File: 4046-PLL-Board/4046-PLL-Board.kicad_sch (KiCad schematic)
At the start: 45 parts, among them J1 Conn_01x02_Pin, J2 Conn_02x03_Odd_Even, J3 Conn_01x02_Pin, J4 Conn_01x02_Pin, J5 Conn_01x02_Pin, J6 Conn_01x03_Pin, U1 CD4046, U2 74LVC2G04, U3 L78M05

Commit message: add IXD614 GDT Driver design REV 1.0.0
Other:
- moved on the sheet: C5, LED1, LED2, R5, R6
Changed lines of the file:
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@@
 	)
 	(junction
-		(at 67.31 167.64)
+		(at 48.26 168.91)
 		(diameter 0)
 		(color 0 0 0 0)
@@
 	(wire
 		(pts
-			(xy 60.96 167.64) (xy 67.31 167.64)
+			(xy 41.91 168.91) (xy 48.26 168.91)
 		)
 		(stroke
@@
 	(wire
 		(pts
-			(xy 87.63 167.64) (xy 81.28 167.64)
+			(xy 68.58 168.91) (xy 62.23 168.91)
 		)
 		(stroke
@@
 	(wire
 		(pts
-			(xy 39.37 167.64) (xy 53.34 167.64)
+			(xy 20.32 168.91) (xy 34.29 168.91)
 		)
 		(stroke
@@
 	(wire
 		(pts
-			(xy 60.96 154.94) (xy 73.66 154.94)
+			(xy 41.91 156.21) (xy 54.61 156.21)
 		)
 		(stroke
@@
 	(wire
 		(pts
-			(xy 87.63 154.94) (xy 81.28 154.94)
+			(xy 68.58 156.21) (xy 62.23 156.21)
 		)
 		(stroke
@@
 	(wire
 		(pts
-			(xy 67.31 167.64) (xy 73.66 167.64)
+			(xy 48.26 168.91) (xy 54.61 168.91)
 		)
 		(stroke
@@
 	)
 	(label "LOCK_STATUS"
-		(at 39.37 167.64 0)
+		(at 20.32 168.91 0)
 		(effects
 			(font
@@
 	(symbol
 		(lib_id "Device:LED")
-		(at 77.47 167.64 180)
+		(at 58.42 168.91 180)
 		(unit 1)
 		(exclude_from_sim no)
@@
 		(fields_autoplaced yes)
 		(property "Reference" "LED2"
-			(at 79.0575 160.02 0)
+			(at 60.0075 161.29 0)
 			(effects
 				(font
@@
 		)
 		(property "Value" "Lock Green"
-			(at 79.0575 162.56 0)
+			(at 60.0075 163.83 0)
 			(effects
 				(font
@@
 		)
 		(property "Footprint" "LED_SMD:LED_0603_1608Metric_Pad1.05x0.95mm_HandSolder"
-			(at 77.47 167.64 0)
+			(at 58.42 168.91 0)
 			(effects
 				(font
@@
 		)
 		(property "Datasheet" "~"
-			(at 77.47 167.64 0)
+			(at 58.42 168.91 0)
 			(effects
 				(font
@@
 		)
 		(property "Description" "Light emitting diode"
-			(at 77.47 167.64 0)
+			(at 58.42 168.91 0)
 			(effects
 				(font
@@
 		)
 		(property "Sim.Pins" "1=K 2=A"
-			(at 77.47 167.64 0)
+			(at 58.42 168.91 0)
 			(effects
 				(font
@@
 	(symbol
 		(lib_id "power:GND")
-		(at 67.31 175.26 0)
+		(at 48.26 176.53 0)
 		(unit 1)
 		(exclude_from_sim no)
@@
 		(fields_autoplaced yes)
 		(property "Reference" "#PWR020"
-			(at 67.31 181.61 0)
+			(at 48.26 182.88 0)
 			(effects
 				(font
@@
 		)
 		(property "Value" "GND"
-			(at 67.31 180.34 0)
+			(at 48.26 181.61 0)
 			(effects
 				(font
@@
 		)
 		(property "Footprint" ""
-			(at 67.31 175.26 0)
+			(at 48.26 176.53 0)
 			(effects
 				(font
@@
 		)
 		(property "Datasheet" ""
-			(at 67.31 175.26 0)
+			(at 48.26 176.53 0)
 			(effects
 				(font
@@
 		)
 		(property "Description" "Power symbol creates a global label with name \"GND\" , ground"
-			(at 67.31 175.26 0)
+			(at 48.26 176.53 0)
 			(effects
 				(font
@@
 	(symbol
 		(lib_id "Device:R")
-		(at 57.15 167.64 90)
+		(at 38.1 168.91 90)
 		(unit 1)
 		(exclude_from_sim no)
@@
 		(fields_autoplaced yes)
 		(property "Reference" "R6"
-			(at 57.15 161.29 90)
+			(at 38.1 162.56 90)
 			(effects
 				(font
@@
 		)
 		(property "Value" "1k"
-			(at 57.15 163.83 90)
+			(at 38.1 165.1 90)
 			(effects
 				(font
@@
 		)
 		(property "Footprint" "Resistor_SMD:R_0603_1608Metric_Pad0.98x0.95mm_HandSolder"
-			(at 57.15 169.418 90)
+			(at 38.1 170.688 90)
 			(effects
 				(font
@@
 		)
 		(property "Datasheet" "~"
-			(at 57.15 167.64 0)
+			(at 38.1 168.91 0)
 			(effects
 				(font
@@
 		)
 		(property "Description" "Resistor"
-			(at 57.15 167.64 0)
+			(at 38.1 168.91 0)
 			(effects
 				(font
@@
 	(symbol
 		(lib_id "Device:R")
-		(at 57.15 154.94 90)
+		(at 38.1 156.21 90)
 		(unit 1)
 		(exclude_from_sim no)
@@
 		(fields_autoplaced yes)
 		(property "Reference" "R5"
-			(at 57.15 148.59 90)
+			(at 38.1 149.86 90)
 			(effects
 				(font
@@
 		)
 		(property "Value" "1k"
-			(at 57.15 151.13 90)
+			(at 38.1 152.4 90)
 			(effects
 				(font
@@
 		)
 		(property "Footprint" "Resistor_SMD:R_0603_1608Metric_Pad0.98x0.95mm_HandSolder"
-			(at 57.15 156.718 90)
+			(at 38.1 157.988 90)
 			(effects
 				(font
@@
 		)
 		(property "Datasheet" "~"
-			(at 57.15 154.94 0)
+			(at 38.1 156.21 0)
 			(effects
 				(font
@@
 		)
 		(property "Description" "Resistor"
-			(at 57.15 154.94 0)
+			(at 38.1 156.21 0)
 			(effects
 				(font
@@
 	(symbol
 		(lib_id "power:GND")
-		(at 87.63 154.94 90)
+		(at 68.58 156.21 90)
 		(unit 1)
 		(exclude_from_sim no)
@@
 		(fields_autoplaced yes)
 		(property "Reference" "#PWR014"
-			(at 93.98 154.94 0)
+			(at 74.93 156.21 0)
 			(effects
 				(font
@@
 		)
 		(property "Value" "GND"
-			(at 91.44 154.9399 90)
+			(at 72.39 156.2099 90)
 			(effects
 				(font
@@
 		)
 		(property "Footprint" ""
-			(at 87.63 154.94 0)
+			(at 68.58 156.21 0)
 			(effects
 				(font
@@
 		)
 		(property "Datasheet" ""
-			(at 87.63 154.94 0)
+			(at 68.58 156.21 0)
 			(effects
 				(font
@@
 		)
 		(property "Description" "Power symbol creates a global label with name \"GND\" , ground"
-			(at 87.63 154.94 0)
+			(at 68.58 156.21 0)
 			(effects
 				(font
@@
 	(symbol
 		(lib_id "Device:LED")
-		(at 77.47 154.94 180)
+		(at 58.42 156.21 180)
 		(unit 1)
 		(exclude_from_sim no)
@@
 		(fields_autoplaced yes)
 		(property "Reference" "LED1"
-			(at 79.0575 147.32 0)
+			(at 60.0075 148.59 0)
 			(effects
 				(font
@@
 		)
 		(property "Value" "PWR Yellow"
-			(at 79.0575 149.86 0)
+			(at 60.0075 151.13 0)
 			(effects
 				(font
@@
 		)
 		(property "Footprint" "LED_SMD:LED_0603_1608Metric_Pad1.05x0.95mm_HandSolder"
-			(at 77.47 154.94 0)
+			(at 58.42 156.21 0)
 			(effects
 				(font
@@
 		)
 		(property "Datasheet" "~"
-			(at 77.47 154.94 0)
+			(at 58.42 156.21 0)
 			(effects
 				(font
@@
 		)
 		(property "Description" "Light emitting diode"
-			(at 77.47 154.94 0)
+			(at 58.42 156.21 0)
 			(effects
 				(font
@@
 		)
 		(property "Sim.Pins" "1=K 2=A"
-			(at 77.47 154.94 0)
+			(at 58.42 156.21 0)
 			(effects
 				(font
@@
 	(symbol
 		(lib_id "power:+5V")
-		(at 53.34 154.94 90)
+		(at 34.29 156.21 90)
 		(unit 1)
 		(exclude_from_sim no)
@@
 		(fields_autoplaced yes)
 		(property "Reference" "#PWR019"
-			(at 57.15 154.94 0)
+			(at 38.1 156.21 0)
 			(effects
 				(font
@@
 		)
 		(property "Value" "+5V"
-			(at 49.53 154.9399 90)
+			(at 30.48 156.2099 90)
 			(effects
 				(font
@@
 		)
 		(property "Footprint" ""
-			(at 53.34 154.94 0)
+			(at 34.29 156.21 0)
 			(effects
 				(font
@@
 		)
 		(property "Datasheet" ""
-			(at 53.34 154.94 0)
+			(at 34.29 156.21 0)
 			(effects
 				(font
@@
 		)
 		(property "Description" "Power symbol creates a global label with name \"+5V\""
-			(at 53.34 154.94 0)
+			(at 34.29 156.21 0)
 			(effects
 				(font
@@
 	(symbol
 		(lib_id "power:GND")
-		(at 87.63 167.64 90)
+		(at 68.58 168.91 90)
 		(unit 1)
 		(exclude_from_sim no)
@@
 		(fields_autoplaced yes)
 		(property "Reference" "#PWR015"
-			(at 93.98 167.64 0)
+			(at 74.93 168.91 0)
 			(effects
 				(font
@@
 		)
 		(property "Value" "GND"
-			(at 91.44 167.6399 90)
+			(at 72.39 168.9099 90)
 			(effects
 				(font
@@
 		)
 		(property "Footprint" ""
-			(at 87.63 167.64 0)
+			(at 68.58 168.91 0)
 			(effects
 				(font
@@
 		)
 		(property "Datasheet" ""
-			(at 87.63 167.64 0)
+			(at 68.58 168.91 0)
 			(effects
 				(font
@@
 		)
 		(property "Description" "Power symbol creates a global label with name \"GND\" , ground"
-			(at 87.63 167.64 0)
+			(at 68.58 168.91 0)
 			(effects
 				(font
@@
 	(symbol
 		(lib_id "Device:C")
-		(at 67.31 171.45 180)
+		(at 48.26 172.72 180)
 		(unit 1)
 		(exclude_from_sim no)
@@
 		(fields_autoplaced yes)
 		(property "Reference" "C5"
-			(at 71.12 170.1799 0)
+			(at 52.07 171.4499 0)
 			(effects
 				(font
@@
 		)
 		(property "Value" "DNP"
-			(at 71.12 172.7199 0)
+			(at 52.07 173.9899 0)
 			(effects
 				(font
@@
 		)
 		(property "Footprint" "Capacitor_SMD:C_0603_1608Metric_Pad1.08x0.95mm_HandSolder"
-			(at 66.3448 167.64 0)
+			(at 47.2948 168.91 0)
 			(effects
 				(font
@@
 		)
 		(property "Datasheet" "~"
-			(at 67.31 171.45 0)
+			(at 48.26 172.72 0)
 			(effects
 				(font
@@
 		)
 		(property "Description" "Unpolarized capacitor"
-			(at 67.31 171.45 0)
+			(at 48.26 172.72 0)
 			(effects
 				(font

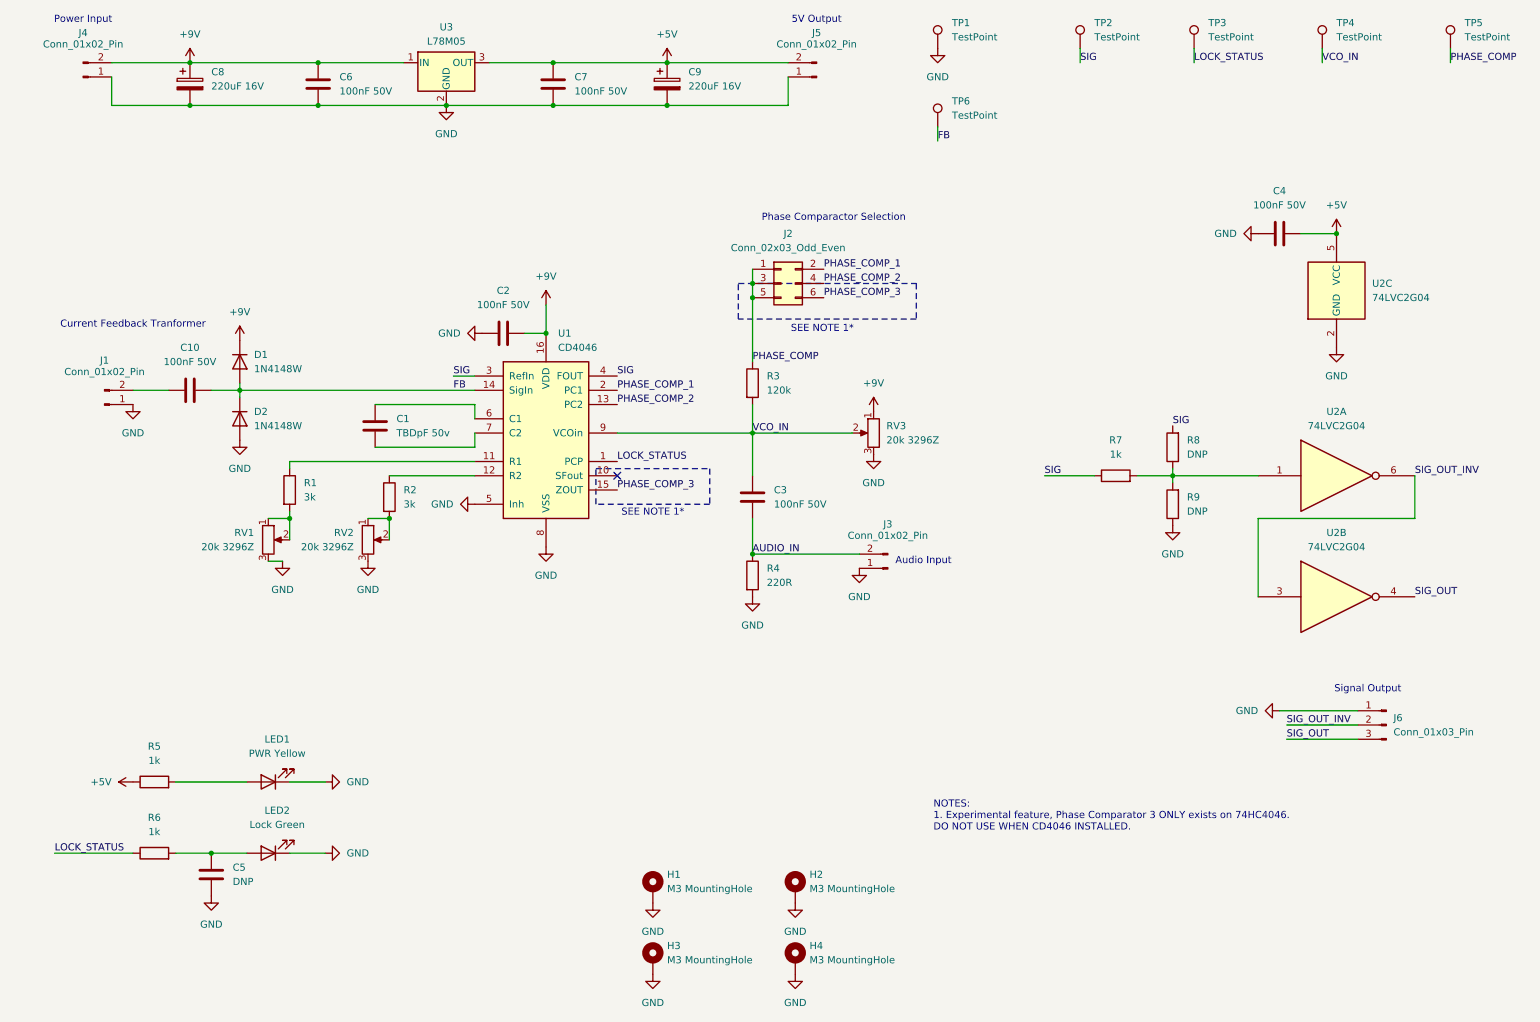
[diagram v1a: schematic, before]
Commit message: add support for CD4046 in SO-16-208mil package on PLL board
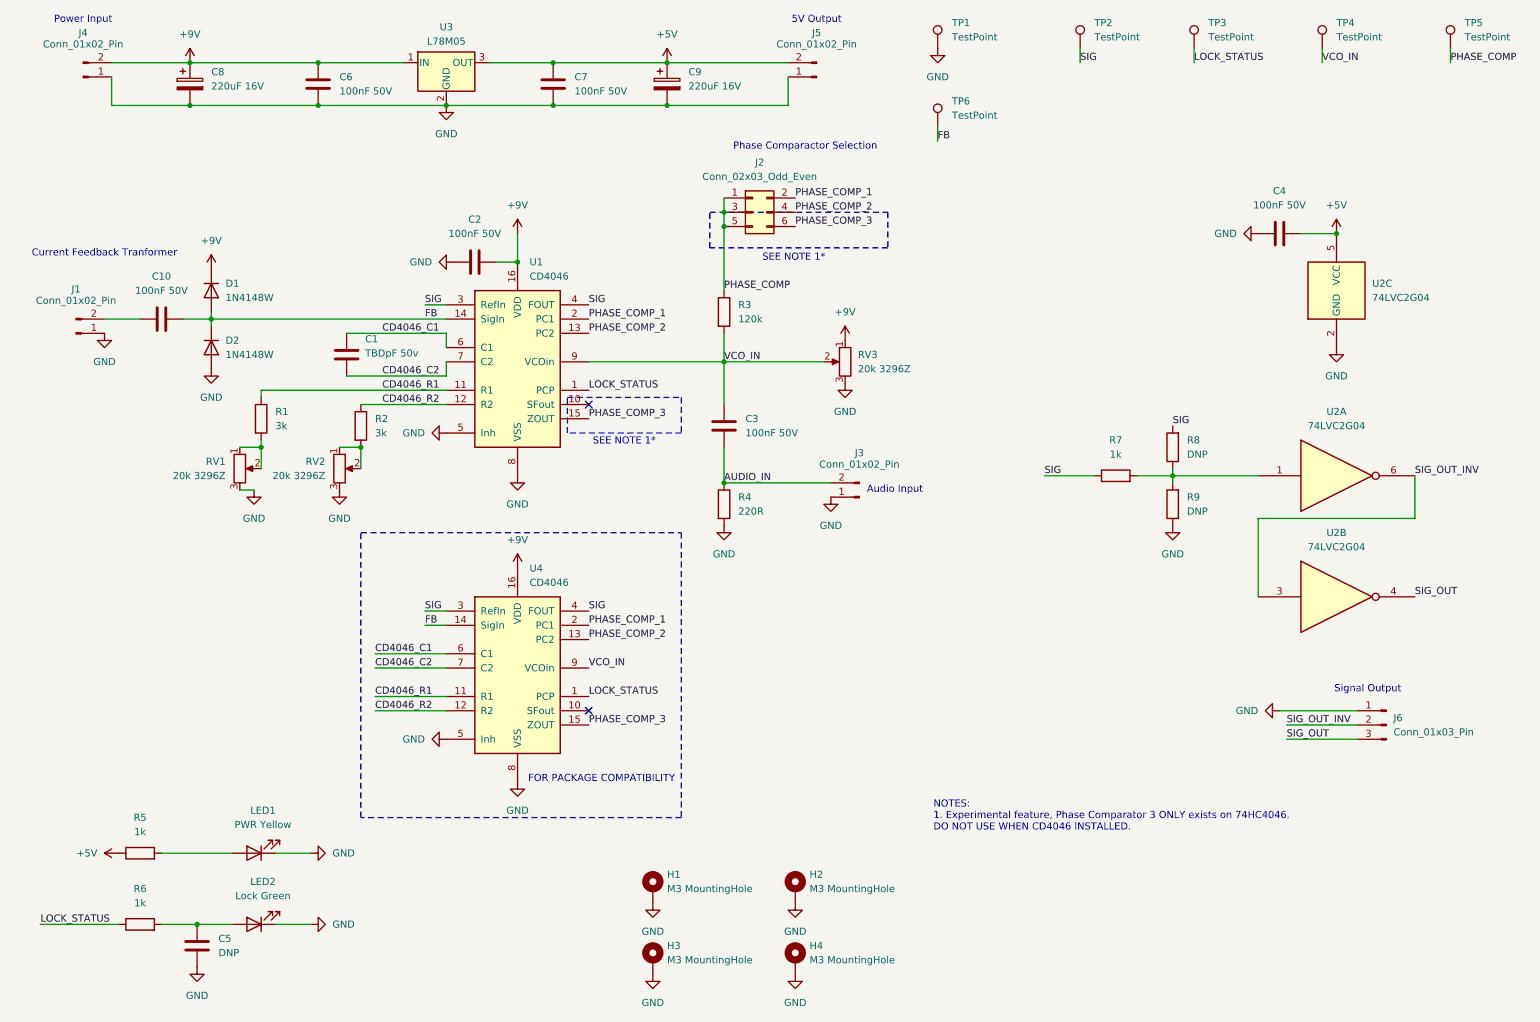
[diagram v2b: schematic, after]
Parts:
- added U4: CD4046, Package_SO:SOIC-16_3.9x9.9mm_P1.27mm, symbol 4xxx:4046
- U1: footprint Package_SO:SOIC-16_3.9x9.9mm_P1.27mm -> Package_SO:SOIC-16_4.55x10.3mm_P1.27mm
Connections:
- net +9V: now also U4.16 (VDD)
- net FB: now also U4.14 (SigIn)
- net GND: now also U4.5 (Inh), U4.8 (VSS)
- net LOCK_STATUS: now also U4.1 (PCP)
- net PHASE_COMP_1: now also U4.2 (PC1)
- net PHASE_COMP_2: now also U4.13 (PC2)
- net PHASE_COMP_3: now also U4.15 (ZOUT)
- net SIG: now also U4.3 (RefIn), U4.4 (FOUT)
- net VCO_IN: now also U4.9 (VCOin)
- net CD4046_R2: now reaches R2.1, U1.12 (R2)
- net CD4046_R2: now also U4.12 (R2)
- net CD4046_C1: now reaches C1.1, U1.6 (C1)
- net CD4046_C1: now also U4.6 (C1)
- net CD4046_C2: now reaches C1.2, U1.7 (C2)
- net CD4046_C2: now also U4.7 (C2)
- net CD4046_R1: now reaches R1.1, U1.11 (R1)
- net CD4046_R1: now also U4.11 (R1)
- no-connect marks 1 -> 2
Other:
- note added: "FOR PACKAGE COMPATIBILITY"
- moved on the sheet: C1, C10, C2, C3, C5, D1, D2, J1, J2, J3, LED1, LED2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
